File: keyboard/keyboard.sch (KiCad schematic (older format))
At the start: 129 parts, among them SW1 `, SW10 0, SW11 -, SW12 =, SW13 Esc, SW14 Tab, SW15 Q, SW16 W, SW17 E, SW18 R, SW19 T, SW2 1, SW20 Y, SW21 U, SW22 I, SW23 O, SW24 P, SW25 [, SW26 ], SW27 \\, SW28 Home, SW29 Hyper, SW3 3, SW30 A, SW31 S, SW32 D, SW33 F, SW34 G, SW35 H, SW36 J, SW37 K, SW38 L, SW39 ;, SW4 4, SW40 ', SW41 Backspace, SW42 Insert, SW43 LShift, SW44 Z, SW45 X, SW46 C, SW47 V, SW48 B, SW49 N, SW5 5, SW51 M, SW52 ,, SW53 ., SW54 /, SW55 Enter, SW56 PageUp, SW57 LCtrl, SW58 Win, SW59 LAlt, SW6 6, SW60 Space, SW61 RAlt, SW62 Menu, SW63 RCtrl, SW64 Print, SW65 2, SW7 7, SW8 8, SW9 9, U1 Elite-C

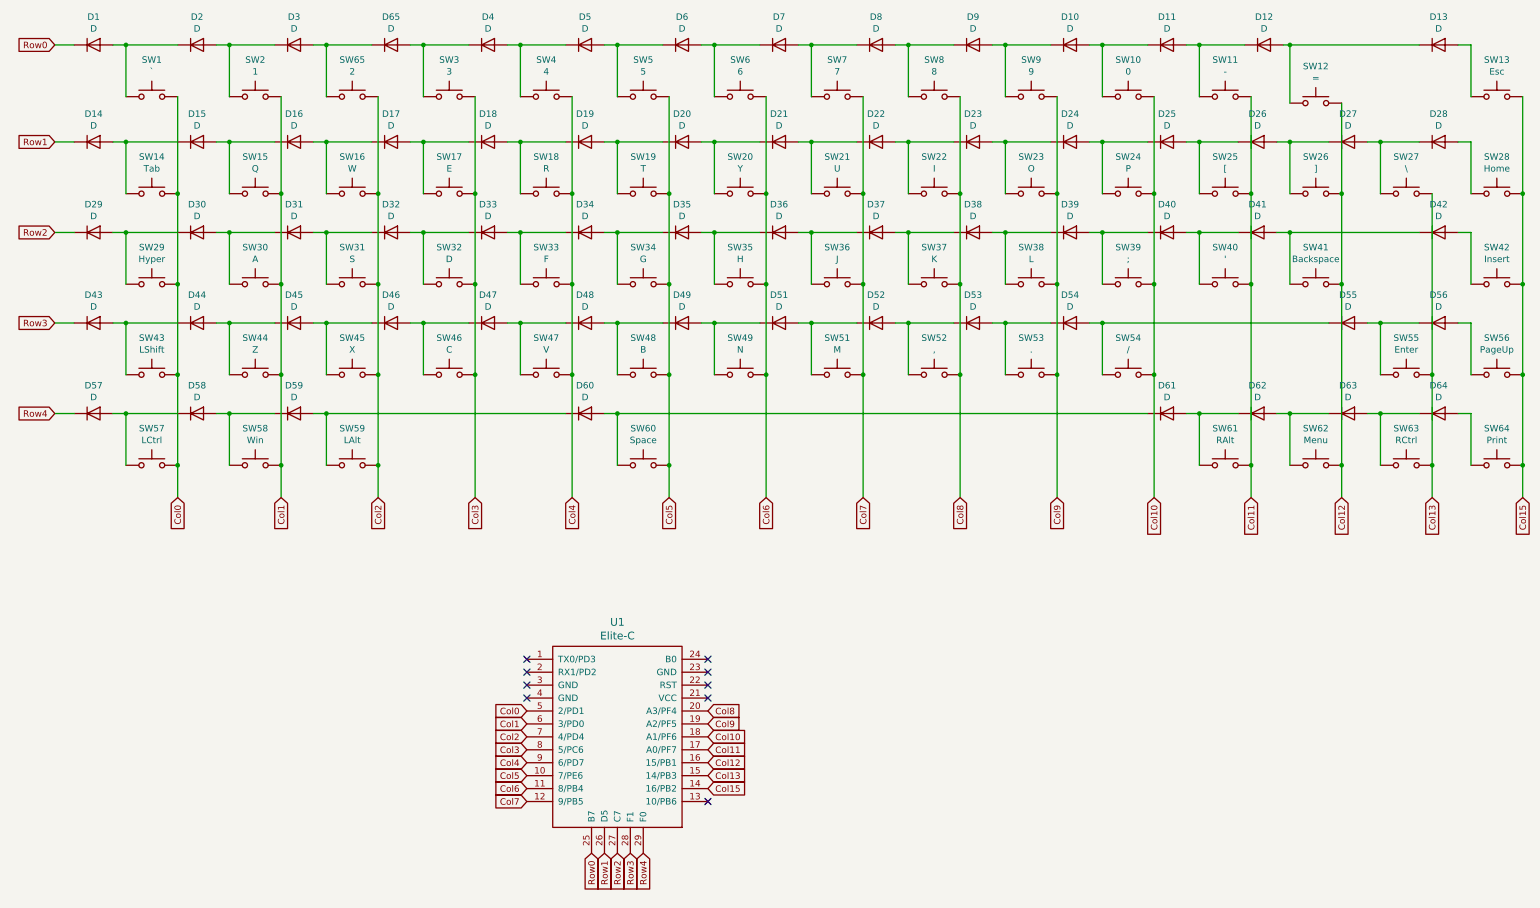
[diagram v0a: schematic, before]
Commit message: completed pcb layout
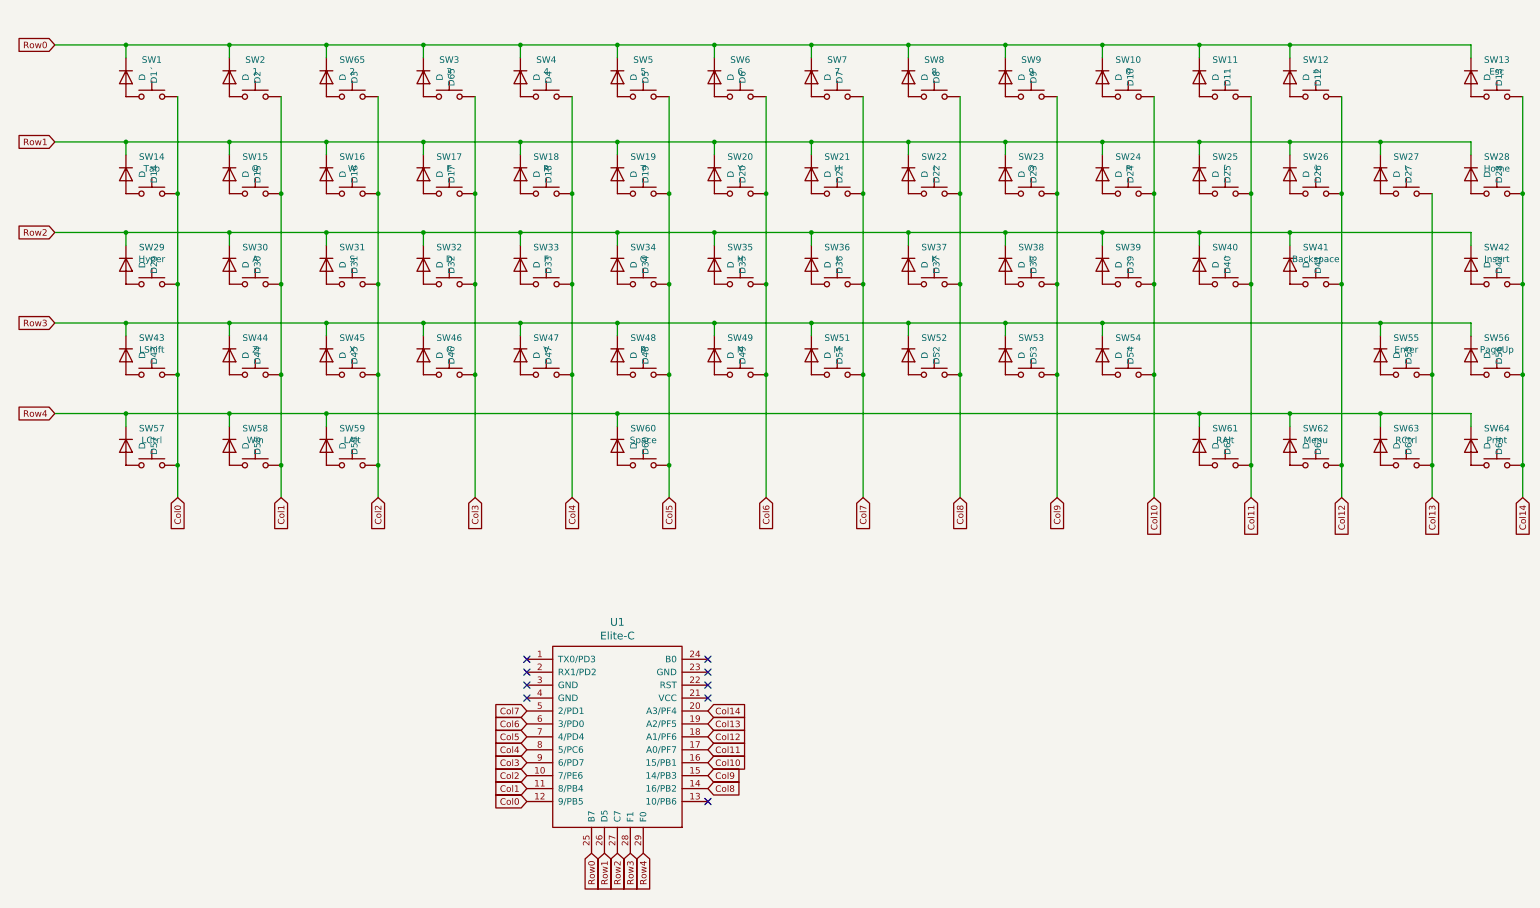
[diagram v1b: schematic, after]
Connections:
- net Col0: now also U1.12 (9/PB5); no longer U1.5 (2/PD1)
- net Col1: now also U1.11 (8/PB4); no longer U1.6 (3/PD0)
- net Col10: now also U1.16 (15/PB1); no longer U1.18 (A1/PF6)
- net Col12: now also U1.18 (A1/PF6); no longer U1.16 (15/PB1)
- net Col13: now also U1.19 (A2/PF5); no longer U1.15 (14/PB3)
- net Col2: now also U1.10 (7/PE6); no longer U1.7 (4/PD4)
- net Col3: now also U1.9 (6/PD7); no longer U1.8 (5/PC6)
- net Col4: now also U1.8 (5/PC6); no longer U1.9 (6/PD7)
- net Col5: now also U1.7 (4/PD4); no longer U1.10 (7/PE6)
- net Col6: now also U1.6 (3/PD0); no longer U1.11 (8/PB4)
- net Col7: now also U1.5 (2/PD1); no longer U1.12 (9/PB5)
- net Col8: now also U1.14 (16/PB2); no longer U1.20 (A3/PF4)
- net Col9: now also U1.15 (14/PB3); no longer U1.19 (A2/PF5)
- net Row0: now also D10.1 (K), D11.1 (K), D12.1 (K), D13.1 (K), D2.1 (K), D3.1 (K), D4.1 (K), D5.1 (K), D6.1 (K), D65.1 (K), D7.1 (K), D8.1 (K), D9.1 (K)
- net Row1: now also D15.1 (K), D16.1 (K), D17.1 (K), D18.1 (K), D19.1 (K), D20.1 (K), D21.1 (K), D22.1 (K), D23.1 (K), D24.1 (K), D25.1 (K), D26.1 (K), D27.1 (K), D28.1 (K)
- net Row2: now also D30.1 (K), D31.1 (K), D32.1 (K), D33.1 (K), D34.1 (K), D35.1 (K), D36.1 (K), D37.1 (K), D38.1 (K), D39.1 (K), D40.1 (K), D41.1 (K), D42.1 (K)
- net Row3: now also D44.1 (K), D45.1 (K), D46.1 (K), D47.1 (K), D48.1 (K), D49.1 (K), D51.1 (K), D52.1 (K), D53.1 (K), D54.1 (K), D55.1 (K), D56.1 (K)
- net Row4: now also D58.1 (K), D59.1 (K), D60.1 (K), D61.1 (K), D62.1 (K), D63.1 (K), D64.1 (K)
- net at D2.2 (A), SW2.1: no longer D3.1 (K)
- net at D65.2 (A), SW3.1: no longer D4.1 (K)
- net at D4.2 (A), SW4.1: no longer D5.1 (K)
- net at D5.2 (A), SW5.1: no longer D6.1 (K)
- net at D6.2 (A), SW6.1: no longer D7.1 (K)
- net at D7.2 (A), SW7.1: no longer D8.1 (K)
- net at D8.2 (A), SW8.1: no longer D9.1 (K)
- net at D9.2 (A), SW9.1: no longer D10.1 (K)
- net at D10.2 (A), SW10.1: no longer D11.1 (K)
- net at D11.2 (A), SW11.1: no longer D12.1 (K)
- net at D12.2 (A), SW12.1: no longer D13.1 (K)
- net at D1.2 (A), SW1.1: no longer D2.1 (K)
- net at D3.2 (A), SW65.1: no longer D65.1 (K)
- net at D14.2 (A), SW14.1: no longer D15.1 (K)
- net at D15.2 (A), SW15.1: no longer D16.1 (K)
- net at D16.2 (A), SW16.1: no longer D17.1 (K)
- net at D17.2 (A), SW17.1: no longer D18.1 (K)
- net at D18.2 (A), SW18.1: no longer D19.1 (K)
- net at D19.2 (A), SW19.1: no longer D20.1 (K)
- net at D20.2 (A), SW20.1: no longer D21.1 (K)
- net at D21.2 (A), SW21.1: no longer D22.1 (K)
- net at D22.2 (A), SW22.1: no longer D23.1 (K)
- net at D23.2 (A), SW23.1: no longer D24.1 (K)
- net at D24.2 (A), SW24.1: no longer D25.1 (K)
- net at D25.2 (A), SW25.1: no longer D26.1 (K)
- net at D26.2 (A), SW26.1: no longer D27.1 (K)
- net at D29.2 (A), SW29.1: no longer D30.1 (K)
- net at D30.2 (A), SW30.1: no longer D31.1 (K)
- net at D31.2 (A), SW31.1: no longer D32.1 (K)
- net at D32.2 (A), SW32.1: no longer D33.1 (K)
- net at D33.2 (A), SW33.1: no longer D34.1 (K)
- net at D34.2 (A), SW34.1: no longer D35.1 (K)
- net at D35.2 (A), SW35.1: no longer D36.1 (K)
- net at D36.2 (A), SW36.1: no longer D37.1 (K)
- net at D37.2 (A), SW37.1: no longer D38.1 (K)
- net at D38.2 (A), SW38.1: no longer D39.1 (K)
- net at D39.2 (A), SW39.1: no longer D40.1 (K)
- net at D40.2 (A), SW40.1: no longer D41.1 (K)
- net at D27.2 (A), SW27.1: no longer D28.1 (K)
- net at D43.2 (A), SW43.1: no longer D44.1 (K)
- net at D44.2 (A), SW44.1: no longer D45.1 (K)
- net at D45.2 (A), SW45.1: no longer D46.1 (K)
- net at D46.2 (A), SW46.1: no longer D47.1 (K)
- net at D47.2 (A), SW47.1: no longer D48.1 (K)
- net at D48.2 (A), SW48.1: no longer D49.1 (K)
- net at D49.2 (A), SW49.1: no longer D51.1 (K)
- net at D51.2 (A), SW51.1: no longer D52.1 (K)
- net at D52.2 (A), SW52.1: no longer D53.1 (K)
- net at D53.2 (A), SW53.1: no longer D54.1 (K)
- net at D41.2 (A), SW41.1: no longer D42.1 (K)
- net at D57.2 (A), SW57.1: no longer D58.1 (K)
- net at D58.2 (A), SW58.1: no longer D59.1 (K)
- net at D59.2 (A), SW59.1: no longer D60.1 (K)
- net at D60.2 (A), SW60.1: no longer D61.1 (K)
- net at D61.2 (A), SW61.1: no longer D62.1 (K)
- net at D62.2 (A), SW62.1: no longer D63.1 (K)
- net at D63.2 (A), SW63.1: no longer D64.1 (K)
- net at D54.2 (A), SW54.1: no longer D55.1 (K)
- net at D55.2 (A), SW55.1: no longer D56.1 (K)
- net Col15 renamed Col14
- net Col14: now also U1.20 (A3/PF4); no longer U1.14 (16/PB2)
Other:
- moved on the sheet: D1, D10, D11, D12, D13, D14, D15, D16, D17, D18, D19, D2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
